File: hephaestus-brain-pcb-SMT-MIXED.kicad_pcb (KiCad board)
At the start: 2 copper layers, 26 x 52 mm, 36 parts, among them IC1 ATSAMD51G19A-MU, J1 Barrel_Jack, J2 Conn_02x03_Odd_Even, J3 StemmaQT, J4 Conn_01x03_Female, J5 Conn_01x03_Male, J6 Conn_01x03_Male, J7 Conn_01x03_Male, J8 USB4110-GF-A, SW1 SW_SPDT, SW2 SW_SPST, SW3 SW_SPST, U1 LM1117-5.0, U2 AP2112K-3.3, U3 AT25xxx-MA, U4 74LVC1G125

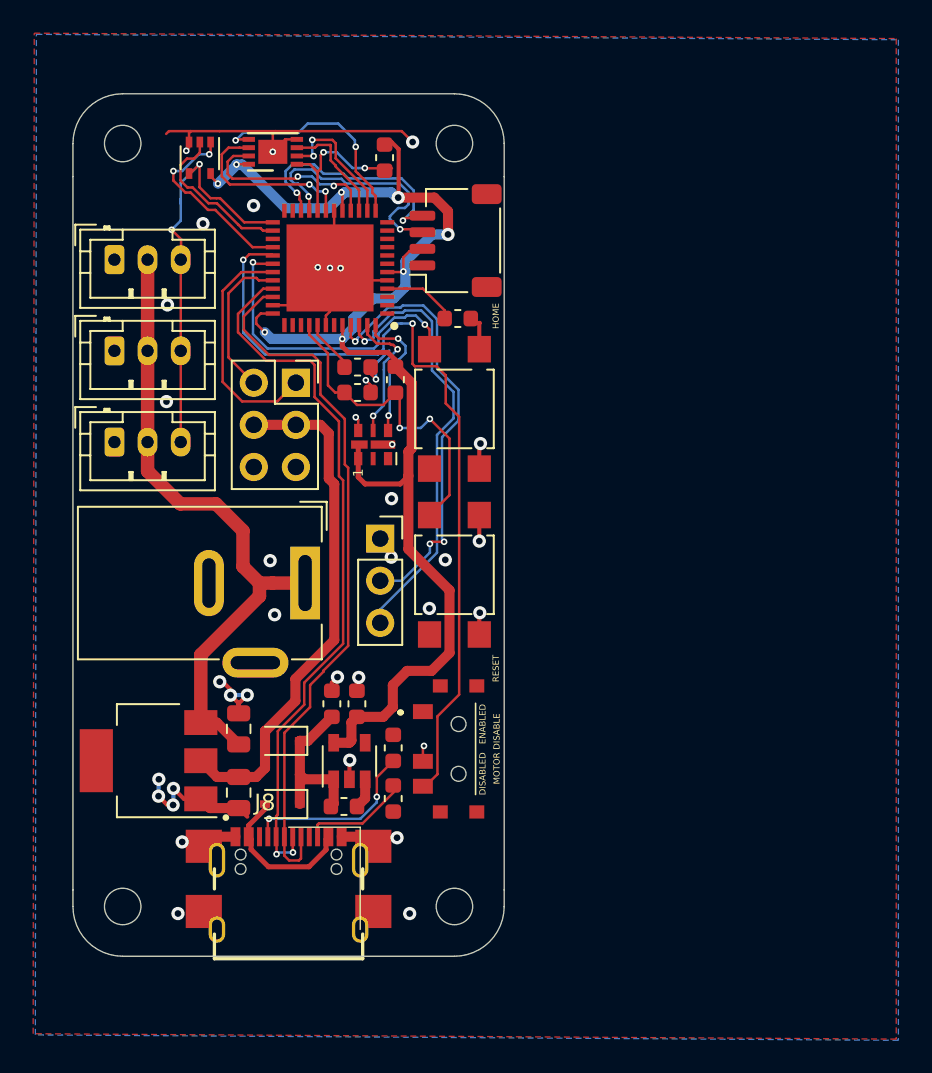
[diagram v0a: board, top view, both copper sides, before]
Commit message: Updated footprints.
0.22mm soldermask clearence on the USB and flash ICs
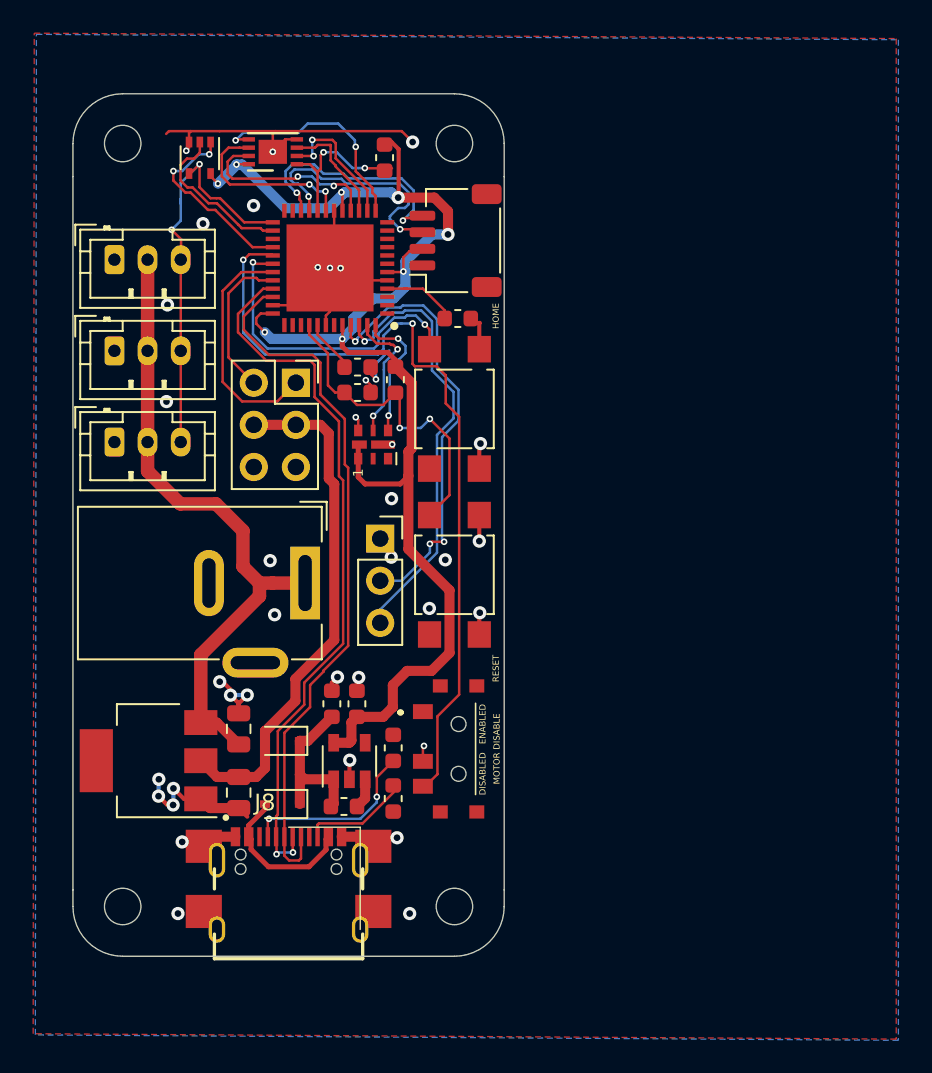
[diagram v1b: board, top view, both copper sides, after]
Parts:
- D3: footprint LED_SMD:LED-APA102-2020 -> unified:LED-APA102-2020
- U3: footprint Package_DFN_QFN:DFN-8-1EP_3x2mm_P0.5mm_EP1.75x1.45mm -> unified:DFN-8-1EP_3x2mm_P0.5mm_EP1.75x1.45mm
